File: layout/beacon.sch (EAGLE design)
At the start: 24 parts, among them IC1 LP2985-SOT23-5, U1 BLE112-A, X1 MINI-USB-SCHIELD-32005-301

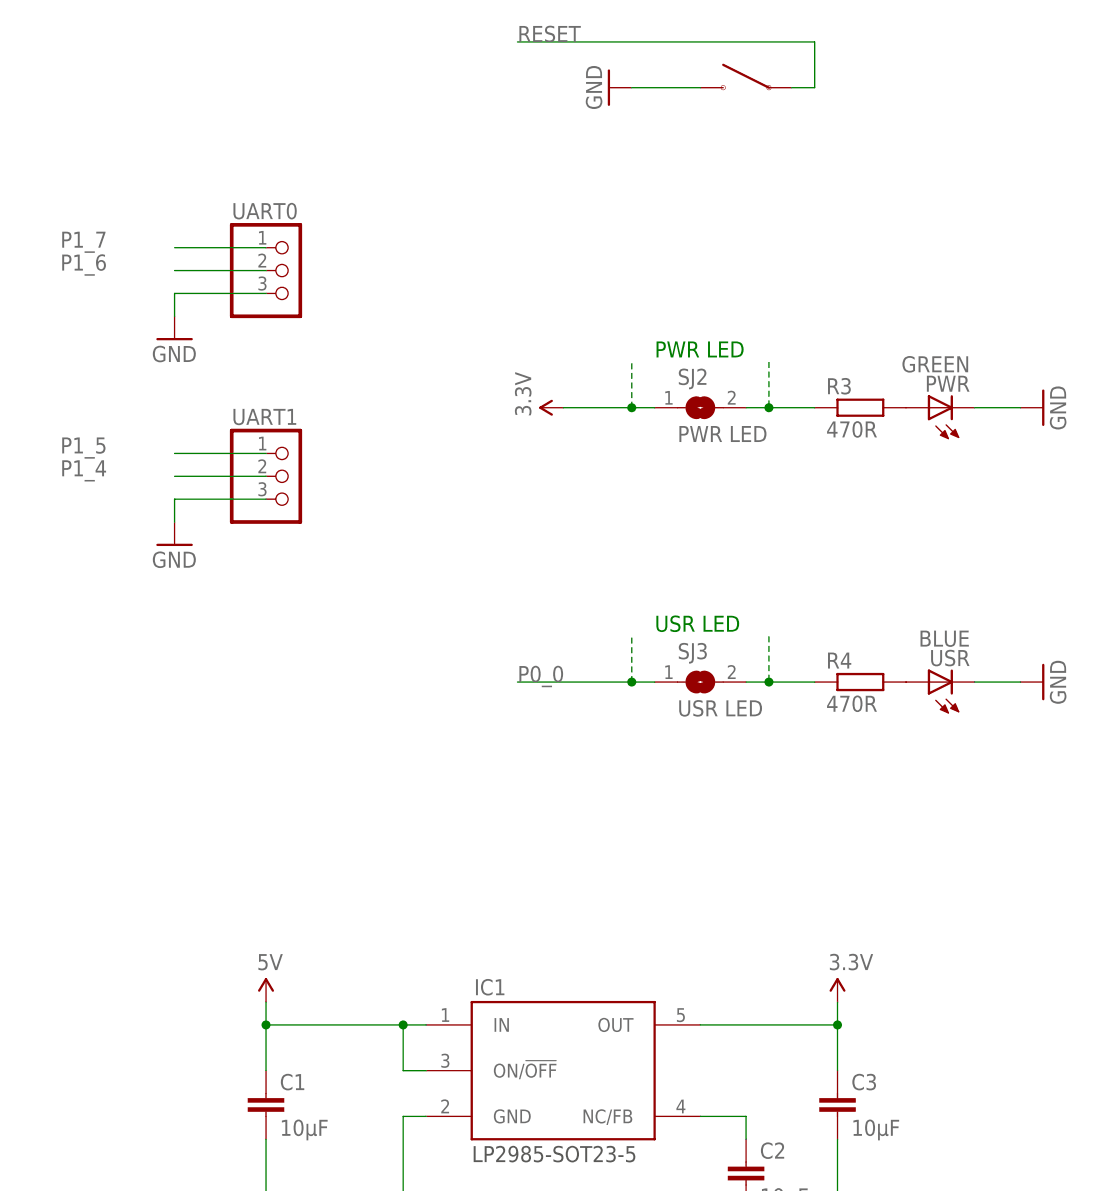
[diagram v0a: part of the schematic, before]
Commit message: Added battery option
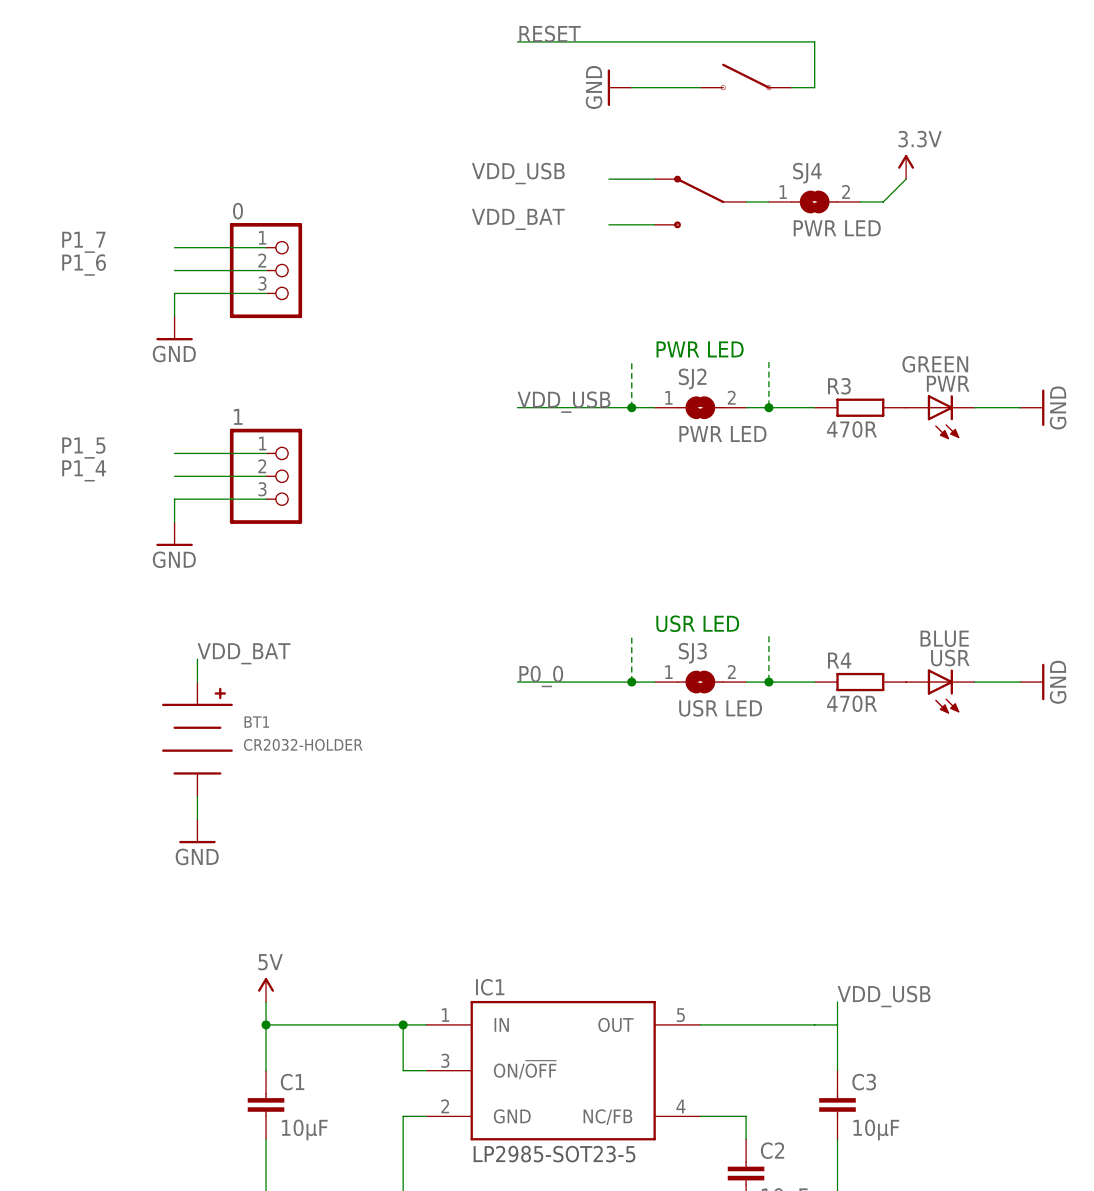
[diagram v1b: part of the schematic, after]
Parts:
- added BT1: CR2032-HOLDER, battery-holder:CR2032-HOLDER
- added SJ4: PWR LED, jumper:SJ
- added U$1: 1P2T, switch:1P2T
- renumbered RESET to RST, UART0 to 0, UART1 to 1
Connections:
- new net N$4: SJ4.1, U$1.P$2
- new net VDD_BAT: BT1.POS, U$1.P$3
- new net VDD_USB: C3.1, IC1.OUT, SJ2.1, U$1.P$1
- net 3.3V: now also SJ4.2; no longer C3.1, IC1.OUT, SJ2.1
- net GND: now also BT1.NEG
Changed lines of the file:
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@@
 <part name="GND11" library="supply1" deviceset="GND" device=""/>
 <part name="GND12" library="supply1" deviceset="GND" device=""/>
-<part name="P+6" library="SparkFun" deviceset="3.3V" device=""/>
 <part name="GND13" library="supply1" deviceset="GND" device=""/>
 <part name="GND14" library="supply1" deviceset="GND" device=""/>
 <part name="X1" library="con-cypressindustries" deviceset="MINI-USB-SCHIELD-" device="32005-301" value=""/>
 <part name="GND16" library="supply1" deviceset="GND" device=""/>
-<part name="RESET" library="tactile-switch" deviceset="TACT-SWITCH-40-40" device=""/>
+<part name="RST" library="tactile-switch" deviceset="TACT-SWITCH-40-40" device=""/>
 <part name="JP3" library="nxp" deviceset="ARM-JTAG" device="_1.27-SMD"/>
 <part name="IC1" library="vreg" deviceset="LP2985" device="-SOT23-5"/>
@@
 <part name="C5" library="rcl" deviceset="C-EU" device="C0603" value="1µF"/>
 <part name="C6" library="rcl" deviceset="C-EU" device="C0603" value="1µF"/>
-<part name="UART0" library="microbuilder" deviceset="HEADER-1X3" device="ROUND"/>
-<part name="UART1" library="microbuilder" deviceset="HEADER-1X3" device="ROUND"/>
+<part name="0" library="microbuilder" deviceset="HEADER-1X3" device="ROUND"/>
+<part name="1" library="microbuilder" deviceset="HEADER-1X3" device="ROUND"/>
 <part name="GND15" library="supply1" deviceset="GND" device=""/>
 <part name="GND17" library="supply1" deviceset="GND" device=""/>
+<part name="U$1" library="switch" deviceset="1P2T" device=""/>
+<part name="BT1" library="battery-holder" deviceset="CR2032-HOLDER" device=""/>
+<part name="GND18" library="supply1" deviceset="GND" device=""/>
+<part name="SJ4" library="jumper" deviceset="SJ" device="" value="PWR LED"/>
 </parts>
 <sheets>
@@
 <instance part="GND11" gate="1" x="35.56" y="91.44" rot="R270"/>
 <instance part="GND12" gate="1" x="50.8" y="175.26" rot="R180"/>
-<instance part="P+6" gate="G$1" x="195.58" y="147.32" rot="R90"/>
 <instance part="GND13" gate="1" x="248.92" y="147.32" rot="R90"/>
 <instance part="GND14" gate="1" x="248.92" y="116.84" rot="R90"/>
@@
 <instance part="X1" gate="S" x="73.66" y="15.24"/>
 <instance part="GND16" gate="1" x="78.74" y="5.08"/>
-<instance part="RESET" gate="G$1" x="215.9" y="182.88"/>
+<instance part="RST" gate="G$1" x="215.9" y="182.88"/>
 <instance part="JP3" gate="A" x="129.54" y="17.78" rot="MR180"/>
 <instance part="IC1" gate="G$1" x="195.58" y="73.66"/>
@@
 <instance part="GND6" gate="1" x="215.9" y="53.34"/>
 <instance part="GND9" gate="1" x="226.06" y="53.34"/>
-<instance part="P+1" gate="G$1" x="226.06" y="81.28"/>
+<instance part="P+1" gate="G$1" x="233.68" y="172.72"/>
 <instance part="U$3" gate="G$1" x="162.56" y="81.28"/>
 <instance part="R1" gate="G$1" x="27.94" y="27.94"/>
@@
 <instance part="C5" gate="G$1" x="111.76" y="91.44" rot="R90"/>
 <instance part="C6" gate="G$1" x="50.8" y="167.64" rot="R180"/>
-<instance part="UART0" gate="A" x="165.1" y="162.56"/>
-<instance part="UART1" gate="A" x="165.1" y="139.7"/>
+<instance part="0" gate="A" x="165.1" y="162.56"/>
+<instance part="1" gate="A" x="165.1" y="139.7"/>
 <instance part="GND15" gate="1" x="152.4" y="154.94"/>
 <instance part="GND17" gate="1" x="152.4" y="132.08"/>
+<instance part="U$1" gate="G$1" x="210.82" y="170.18"/>
+<instance part="BT1" gate="G$1" x="154.94" y="109.22"/>
+<instance part="GND18" gate="1" x="154.94" y="99.06"/>
+<instance part="SJ4" gate="1" x="223.52" y="170.18"/>
 </instances>
 <busses>
@@
 <segment>
 <pinref part="GND5" gate="1" pin="GND"/>
-<pinref part="RESET" gate="G$1" pin="P$1"/>
+<pinref part="RST" gate="G$1" pin="P$1"/>
 <wire x1="203.2" y1="182.88" x2="210.82" y2="182.88" width="0.1524" layer="91"/>
 </segment>
@@
 </segment>
 <segment>
-<pinref part="UART1" gate="A" pin="3"/>
+<pinref part="1" gate="A" pin="3"/>
 <wire x1="162.56" y1="137.16" x2="152.4" y2="137.16" width="0.1524" layer="91"/>
 <wire x1="152.4" y1="137.16" x2="152.4" y2="134.62" width="0.1524" layer="91"/>
@@
 </segment>
 <segment>
-<pinref part="UART0" gate="A" pin="3"/>
+<pinref part="0" gate="A" pin="3"/>
 <wire x1="162.56" y1="160.02" x2="152.4" y2="160.02" width="0.1524" layer="91"/>
 <wire x1="152.4" y1="160.02" x2="152.4" y2="157.48" width="0.1524" layer="91"/>
 <pinref part="GND15" gate="1" pin="GND"/>
 </segment>
+<segment>
+<pinref part="GND18" gate="1" pin="GND"/>
+<pinref part="BT1" gate="G$1" pin="NEG"/>
+<wire x1="154.94" y1="101.6" x2="154.94" y2="104.14" width="0.1524" layer="91"/>
+</segment>
 </net>
 <net name="P1_5" class="0">
@@
 </segment>
 <segment>
-<pinref part="UART1" gate="A" pin="1"/>
+<pinref part="1" gate="A" pin="1"/>
 <wire x1="162.56" y1="142.24" x2="152.4" y2="142.24" width="0.1524" layer="91"/>
 <label x="139.7" y="142.24" size="1.778" layer="95"/>
@@
 </segment>
 <segment>
-<pinref part="UART0" gate="A" pin="2"/>
+<pinref part="0" gate="A" pin="2"/>
 <wire x1="162.56" y1="162.56" x2="152.4" y2="162.56" width="0.1524" layer="91"/>
 <label x="139.7" y="162.56" size="1.778" layer="95"/>
@@
 </segment>
 <segment>
-<pinref part="UART0" gate="A" pin="1"/>
+<pinref part="0" gate="A" pin="1"/>
 <wire x1="162.56" y1="165.1" x2="152.4" y2="165.1" width="0.1524" layer="91"/>
 <label x="139.7" y="165.1" size="1.778" layer="95"/>
@@
 <wire x1="190.5" y1="187.96" x2="223.52" y2="187.96" width="0.1524" layer="91"/>
 <wire x1="223.52" y1="187.96" x2="223.52" y2="182.88" width="0.1524" layer="91"/>
-<pinref part="RESET" gate="G$1" pin="P$2"/>
+<pinref part="RST" gate="G$1" pin="P$2"/>
 <wire x1="223.52" y1="182.88" x2="220.98" y2="182.88" width="0.1524" layer="91"/>
 </segment>
@@
 </segment>
 <segment>
-<pinref part="SJ2" gate="1" pin="1"/>
-<wire x1="205.74" y1="147.32" x2="203.2" y2="147.32" width="0.1524" layer="91"/>
-<wire x1="203.2" y1="147.32" x2="195.58" y2="147.32" width="0.1524" layer="91"/>
-<wire x1="203.2" y1="147.32" x2="203.2" y2="152.4" width="0.1524" layer="91" style="shortdash"/>
-<junction x="203.2" y="147.32"/>
-<pinref part="P+6" gate="G$1" pin="3.3V"/>
-</segment>
-<segment>
-<pinref part="IC1" gate="G$1" pin="OUT"/>
-<wire x1="210.82" y1="78.74" x2="226.06" y2="78.74" width="0.1524" layer="91"/>
-<wire x1="226.06" y1="78.74" x2="226.06" y2="81.28" width="0.1524" layer="91"/>
-<pinref part="C3" gate="G$1" pin="1"/>
-<wire x1="226.06" y1="78.74" x2="226.06" y2="73.66" width="0.1524" layer="91"/>
-<junction x="226.06" y="78.74"/>
 <pinref part="P+1" gate="G$1" pin="3.3V"/>
+<wire x1="231.14" y1="170.18" x2="233.68" y2="172.72" width="0.1524" layer="91"/>
+<pinref part="SJ4" gate="1" pin="2"/>
+<wire x1="228.6" y1="170.18" x2="231.14" y2="170.18" width="0.1524" layer="91"/>
 </segment>
 </net>
@@
 </segment>
 <segment>
-<pinref part="UART1" gate="A" pin="2"/>
+<pinref part="1" gate="A" pin="2"/>
 <wire x1="162.56" y1="139.7" x2="152.4" y2="139.7" width="0.1524" layer="91"/>
 <label x="139.7" y="139.7" size="1.778" layer="95"/>
@@
 </segment>
 </net>
+<net name="VDD_USB" class="0">
+<segment>
+<pinref part="IC1" gate="G$1" pin="OUT"/>
+<wire x1="210.82" y1="78.74" x2="223.52" y2="78.74" width="0.1524" layer="91"/>
+<pinref part="C3" gate="G$1" pin="1"/>
+<wire x1="226.06" y1="78.74" x2="226.06" y2="73.66" width="0.1524" layer="91"/>
+<wire x1="223.52" y1="78.74" x2="226.06" y2="78.74" width="0.1524" layer="91"/>
+<wire x1="226.06" y1="78.74" x2="226.06" y2="81.28" width="0.1524" layer="91"/>
+<label x="226.06" y="81.28" size="1.778" layer="95"/>
+</segment>
+<segment>
+<pinref part="SJ2" gate="1" pin="1"/>
+<wire x1="205.74" y1="147.32" x2="203.2" y2="147.32" width="0.1524" layer="91"/>
+<wire x1="203.2" y1="147.32" x2="190.5" y2="147.32" width="0.1524" layer="91"/>
+<wire x1="203.2" y1="147.32" x2="203.2" y2="152.4" width="0.1524" layer="91" style="shortdash"/>
+<junction x="203.2" y="147.32"/>
+<label x="190.5" y="147.32" size="1.778" layer="95"/>
+</segment>
+<segment>
+<pinref part="U$1" gate="G$1" pin="P$1"/>
+<wire x1="205.74" y1="172.72" x2="200.66" y2="172.72" width="0.1524" layer="91"/>
+<label x="185.42" y="172.72" size="1.778" layer="95"/>
+</segment>
+</net>
+<net name="VDD_BAT" class="0">
+<segment>
+<pinref part="U$1" gate="G$1" pin="P$3"/>
+<wire x1="205.74" y1="167.64" x2="200.66" y2="167.64" width="0.1524" layer="91"/>
+<label x="185.42" y="167.64" size="1.778" layer="95"/>
+</segment>
+<segment>
+<pinref part="BT1" gate="G$1" pin="POS"/>
+<wire x1="154.94" y1="116.84" x2="154.94" y2="119.38" width="0.1524" layer="91"/>
+<label x="154.94" y="119.38" size="1.778" layer="95"/>
+</segment>
+</net>
+<net name="N$4" class="0">
+<segment>
+<pinref part="U$1" gate="G$1" pin="P$2"/>
+<pinref part="SJ4" gate="1" pin="1"/>
+<wire x1="215.9" y1="170.18" x2="218.44" y2="170.18" width="0.1524" layer="91"/>
+</segment>
+</net>
